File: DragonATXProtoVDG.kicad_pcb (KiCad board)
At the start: 2 copper layers, 161.3 x 85.5 mm, 71 parts, among them IC1 74LS273, IC2 MC6847, IC3 MC14053, J1 Video Output, J2 Board Interconnect Male, J3 JTAG, Q1 MMBT4401, Q2 NPN, Q3 NPN, Q4 NPN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

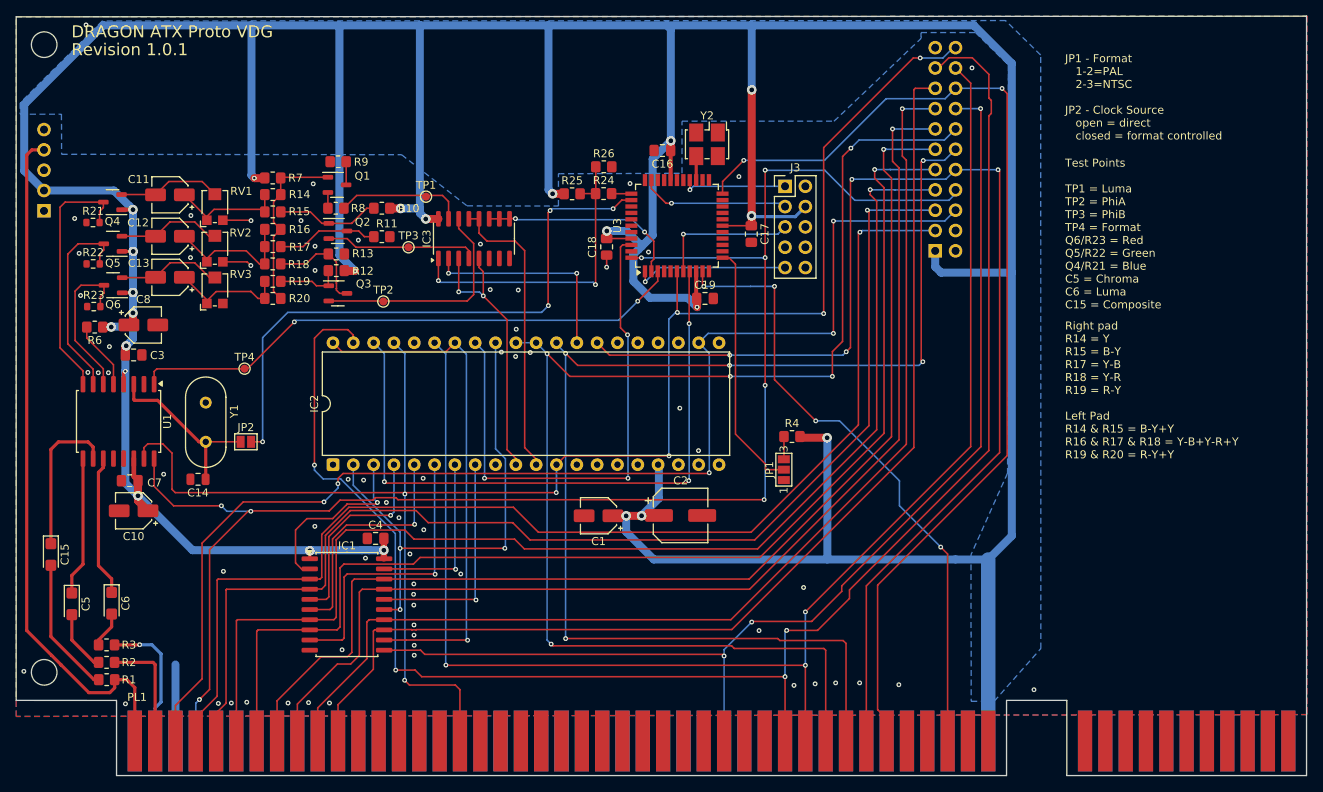
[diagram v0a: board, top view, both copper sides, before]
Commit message: rework for path gates
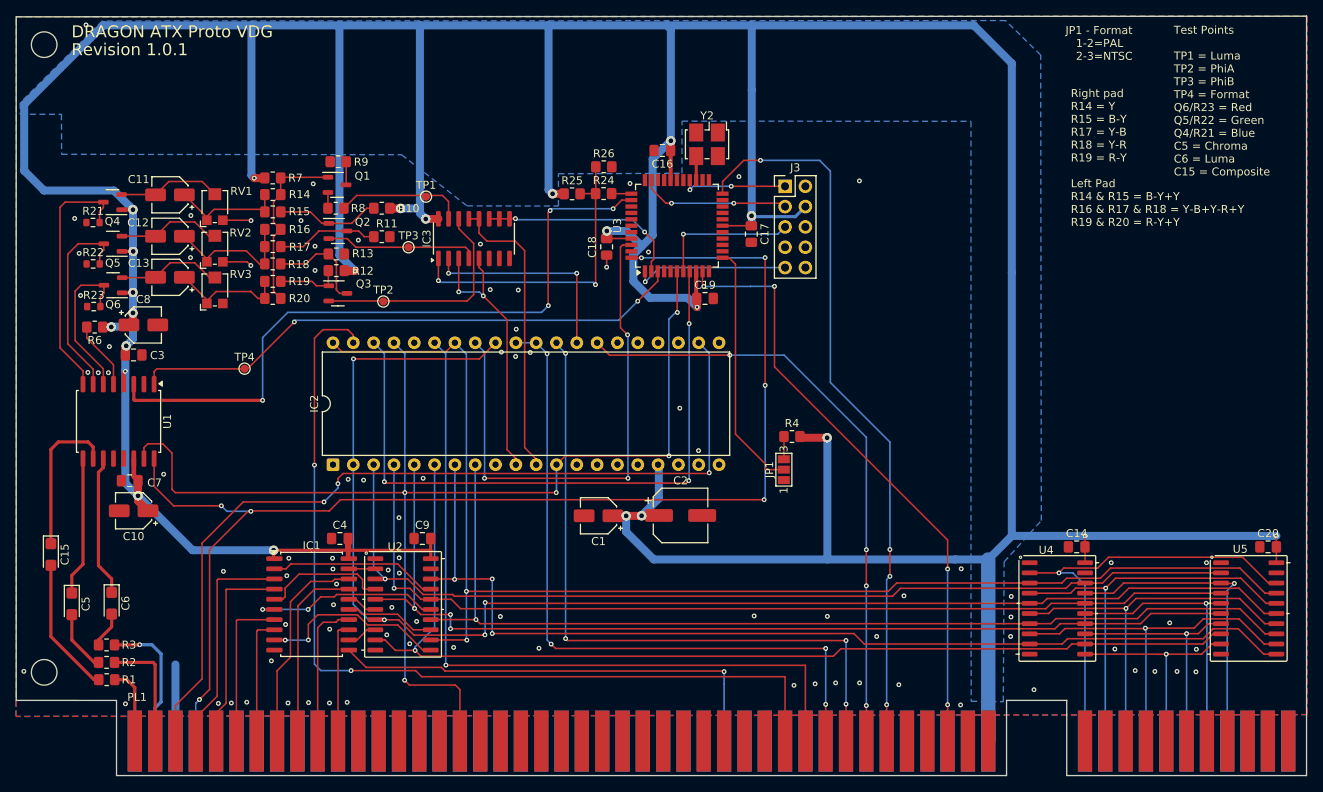
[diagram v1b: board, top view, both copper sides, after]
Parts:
- removed J1: Video Output, Connector_PinHeader_2.54mm:PinHeader_1x05_P2.54mm_Vertical
- removed J2: Board Interconnect Male, Connector_PinHeader_2.54mm:PinHeader_2x11_P2.54mm_Vertical
- removed JP2: FormatClock, Jumper:SolderJumper-2_P1.3mm_Open_Pad1.0x1.5mm
- removed Y1: 4.433620MHz, Crystal:Crystal_HC18-U_Vertical
- added C20: 0.1uF, Capacitor_SMD:C_0805_2012Metric_Pad1.18x1.45mm_HandSolder, F.Cu at (220.4, 90.9)
- added C9: 0.1uF, Capacitor_SMD:C_0805_2012Metric_Pad1.18x1.45mm_HandSolder, F.Cu at (114.7, 89.8)
- added U2: 74LS244, PCM_Package_SO_AKL:SO-20_5.3x12.6mm_P1.27mm, F.Cu at (112.2, 98.0)
- added U4: 74LS244, PCM_Package_SO_AKL:SO-20_5.3x12.6mm_P1.27mm, F.Cu at (194.0, 98.6)
- added U5: 74LS244, PCM_Package_SO_AKL:SO-20_5.3x12.6mm_P1.27mm, F.Cu at (217.9, 98.6)
- C14: value 51pF -> 0.1uF; footprint Capacitor_SMD:C_0805_2012Metric -> Capacitor_SMD:C_0805_2012Metric_Pad1.18x1.45mm_HandSolder
- moved C14 110.2 mm to (196.4, 90.9), turned to 0 degrees
- moved C4 4.46 mm to (104.3, 89.8)
- moved IC1 4.42 mm to (100.8, 98.0)
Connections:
- net ~{FS} renamed /~{FS}
- C14 pad 1: Net-(JP2-A) -> GND
- C14 pad 2: GND -> +5V
- IC1 pad 12: /Q7 -> Net-(IC1-Q4)
- IC1 pad 15: /Q6 -> Net-(IC1-Q5)
- IC1 pad 16: /Q5 -> Net-(IC1-Q6)
- IC1 pad 19: /Q4 -> Net-(IC1-Q7)
- IC1 pad 2: /Q0 -> Net-(IC1-Q0)
- IC1 pad 5: /Q1 -> Net-(IC1-Q1)
- IC1 pad 6: /Q2 -> Net-(IC1-Q2)
- IC1 pad 9: /Q3 -> Net-(IC1-Q3)
- IC3 pad 11: LUM CONTROL -> GND
- IC3 pad 12: phiA -> GND
- IC3 pad 13: phiA -> GND
- IC3 pad 14: phiA' -> unconnected-(IC3-X-Pad14)
- IC3 pad 3: phiB -> GND
- IC3 pad 4: phiB' -> unconnected-(IC3-Z-Pad4)
- IC3 pad 5: phiB -> GND
- IC3 pad 9: LUM CONTROL -> GND
- U1 pad 3: Net-(JP2-A) -> FMT_CLOCK
- U3 pad 31: SYNC_CONTROL -> unconnected-(U3-I/O-Pad31)
- U3 pad 33: CHROMA_CONTROL -> unconnected-(U3-I/O-Pad33)
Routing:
- net /DL3: track 147.7 -> 15.9 mm, vias 1 -> 0
- net /DL2: track 151.1 -> 19.7 mm, vias 1 -> 0
- net /DL1: track 150.5 -> 25.4 mm, vias 1 -> 0
- net /DL7: track 140.1 -> 15.1 mm
- net /DL6: track 140.3 -> 18.3 mm, vias 1 -> 0
- net /DL0: track 148.8 -> 28.3 mm, vias 1 -> 0
- net /DL5: track 142.7 -> 24.0 mm, vias 1 -> 0
- net /DL4: track 143.5 -> 26.5 mm, vias 1 -> 0
- net /Q6: track 61.9 -> 173.6 mm, vias 3 -> 4
- net /Q4: track 22.1 -> 129.6 mm, vias 1 -> 3
- net /Q0: track 22.8 -> 122.7 mm
- net /Q5: track 28.5 -> 127.4 mm
- net /Q7: track 64.4 -> 162.2 mm, vias 1 -> 2
- net /Q2: track 30.0 -> 127.0 mm, vias 1 -> 3
- net /Q1: track 25.4 -> 120.7 mm
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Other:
- board text added: "JP1 - Format 1-2=PAL 2-3=NTSC"
- board text removed: "JP1 - Format 1-2=PAL 2-3=NTSC JP2 - Clock Source open = direct closed = format controlled"

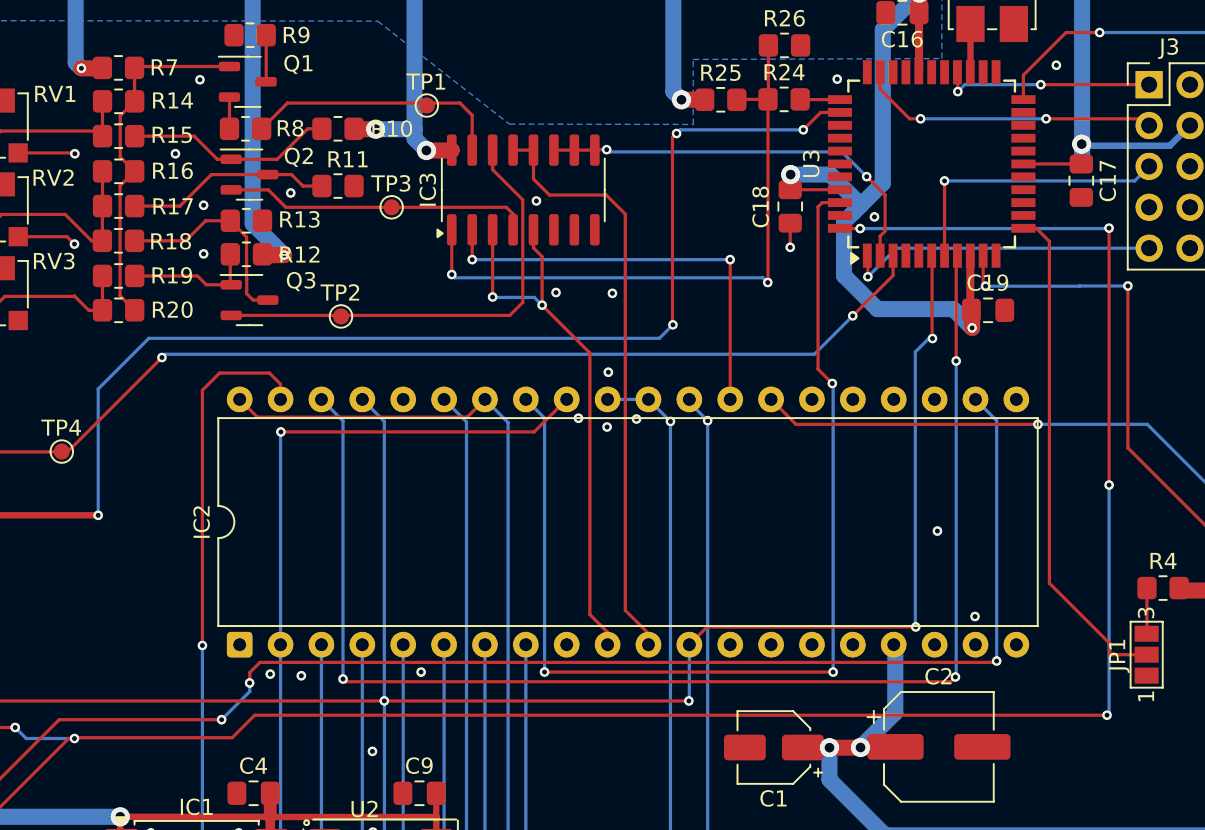
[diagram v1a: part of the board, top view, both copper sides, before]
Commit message: revise cpld logic
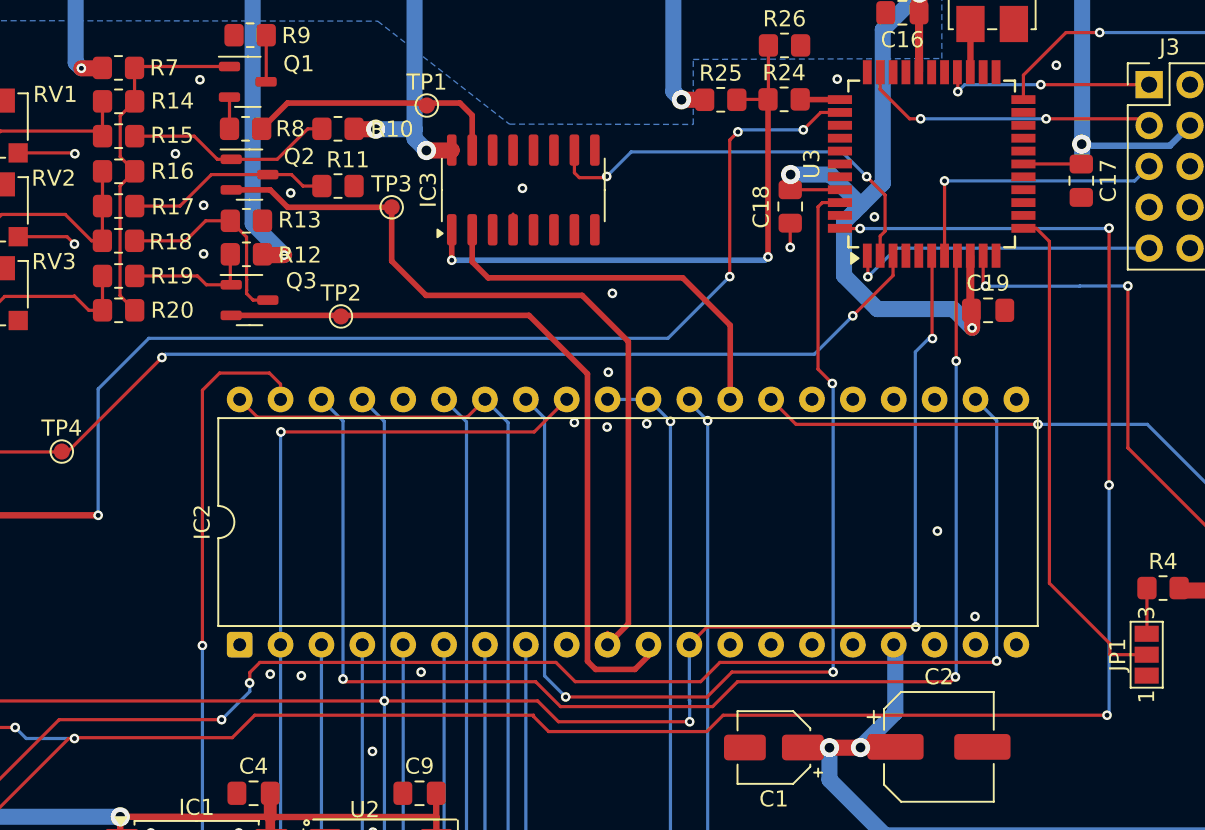
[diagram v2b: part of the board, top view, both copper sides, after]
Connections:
- Q2 pad 2: phiB' -> phiB
- Q3 pad 2: phiA' -> phiA
- TP2 pad 1: phiA' -> phiA
- TP3 pad 1: phiB' -> phiB
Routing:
- net phiA': track 28.7 -> 0.00 mm
- net phiB': track 19.1 -> 0.00 mm
- net phiB: track 35.1 -> 50.7 mm, vias 2 -> 0
- net phiA: track 37.0 -> 47.2 mm
- net PadLuma: track 39.3 -> 36.7 mm
- net LUM: track 26.6 -> 24.3 mm, vias 2 -> 0
- net FMT_CLOCK: track 86.0 -> 84.1 mm
- net /~{FS}: track 156.8 -> 158.7 mm
- net CLK: track 66.1 -> 67.5 mm
- net ~{HS}: track 82.4 -> 83.7 mm
- net /DA0: track 110.7 -> 111.7 mm
- net unconnected-(IC3-Z-Pad4): track 0.00 -> 0.97 mm
- net /HS: track 160.4 -> 161.3 mm
- net LUM CONTROL: track 25.6 -> 26.5 mm
- net GND: track 18.3 -> 18.4 mm, vias 89 -> 88
